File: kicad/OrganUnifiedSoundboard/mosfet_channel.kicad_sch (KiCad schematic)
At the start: 4 parts

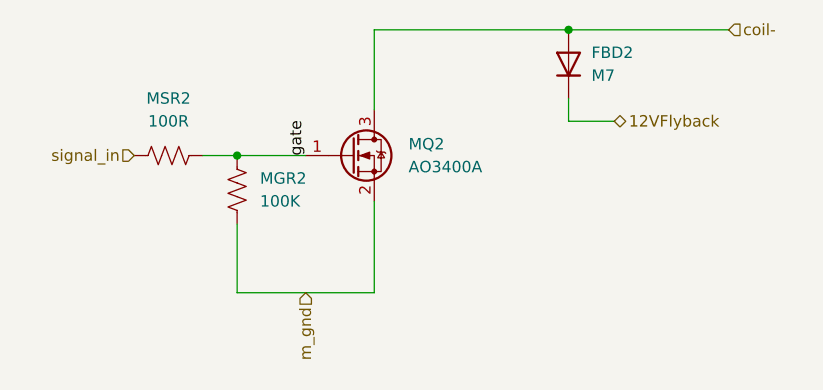
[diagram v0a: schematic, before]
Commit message: Finalized unified soundboard driver for production, adding some models
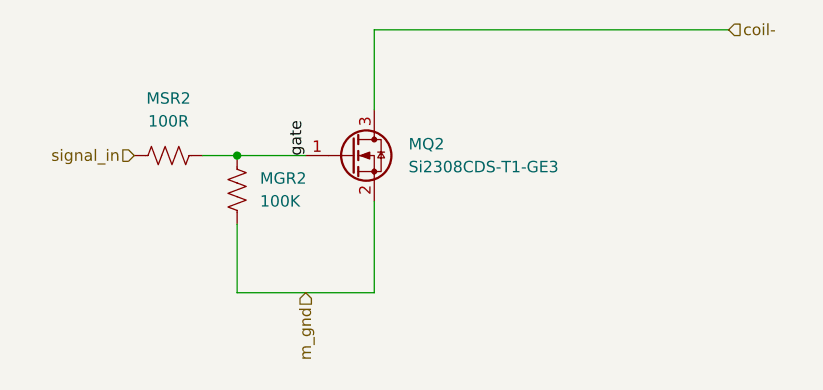
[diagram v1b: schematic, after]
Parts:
- removed FBD2: M7, Diode_SMD:D_SMA, symbol Device:D
- MQ2: value AO3400A -> Si2308CDS-T1-GE3
